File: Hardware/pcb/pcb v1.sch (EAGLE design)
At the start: 1 part, among them Y1 CFS206

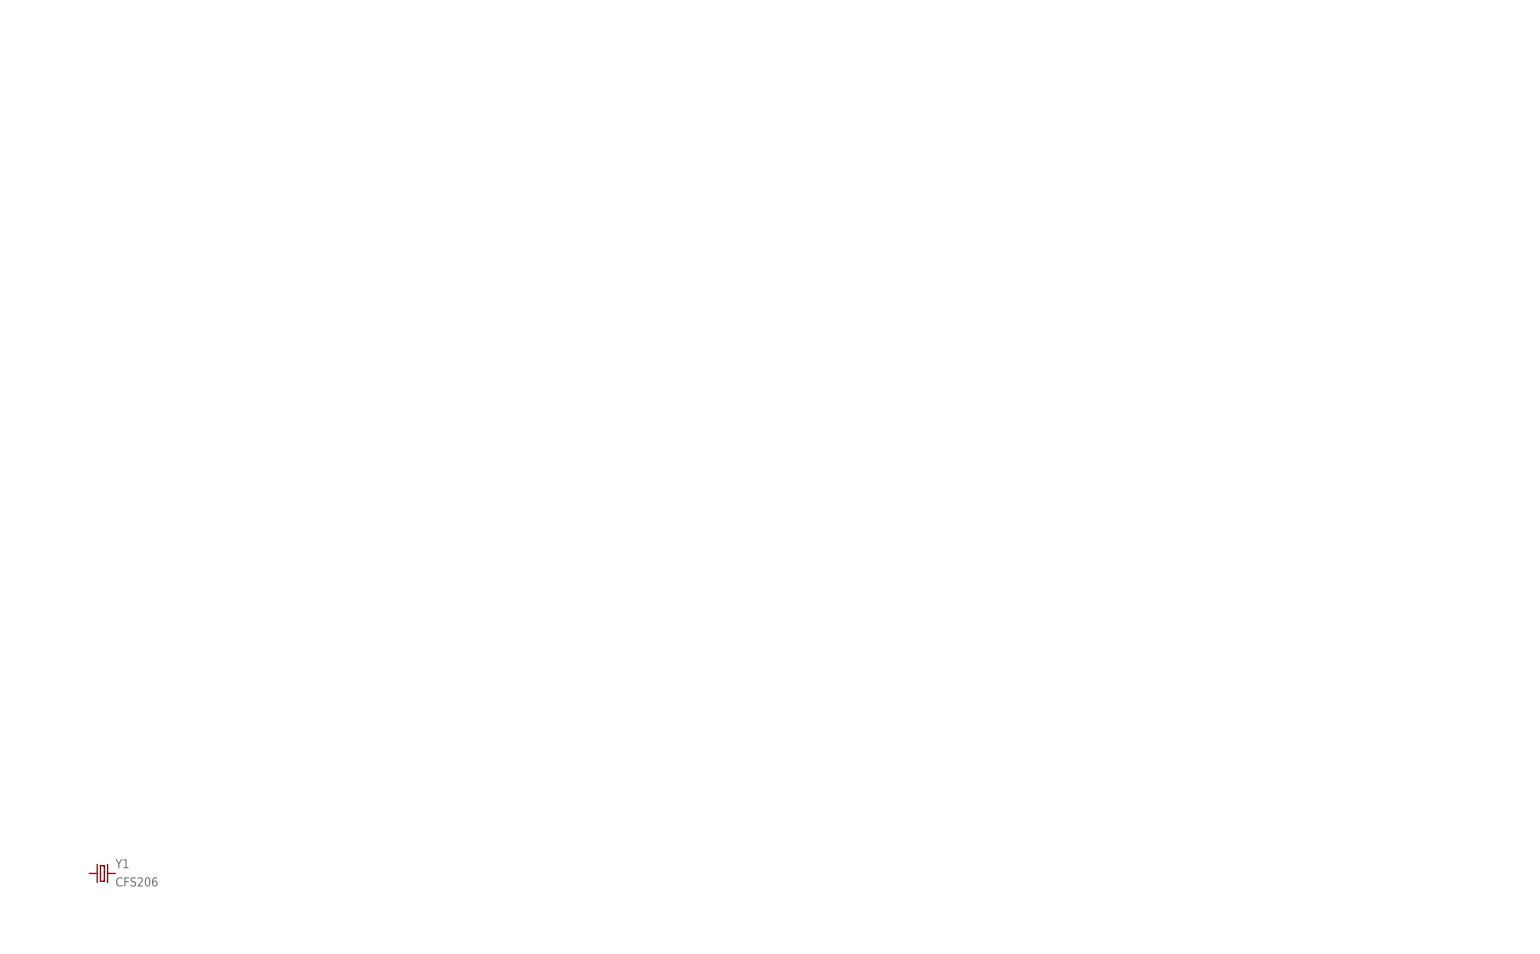
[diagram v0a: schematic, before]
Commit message: Perifericos agregados
Modulo Grove RFID
RTC
2 Reles
Regulador 3.3v
Buzzer
LED RGB
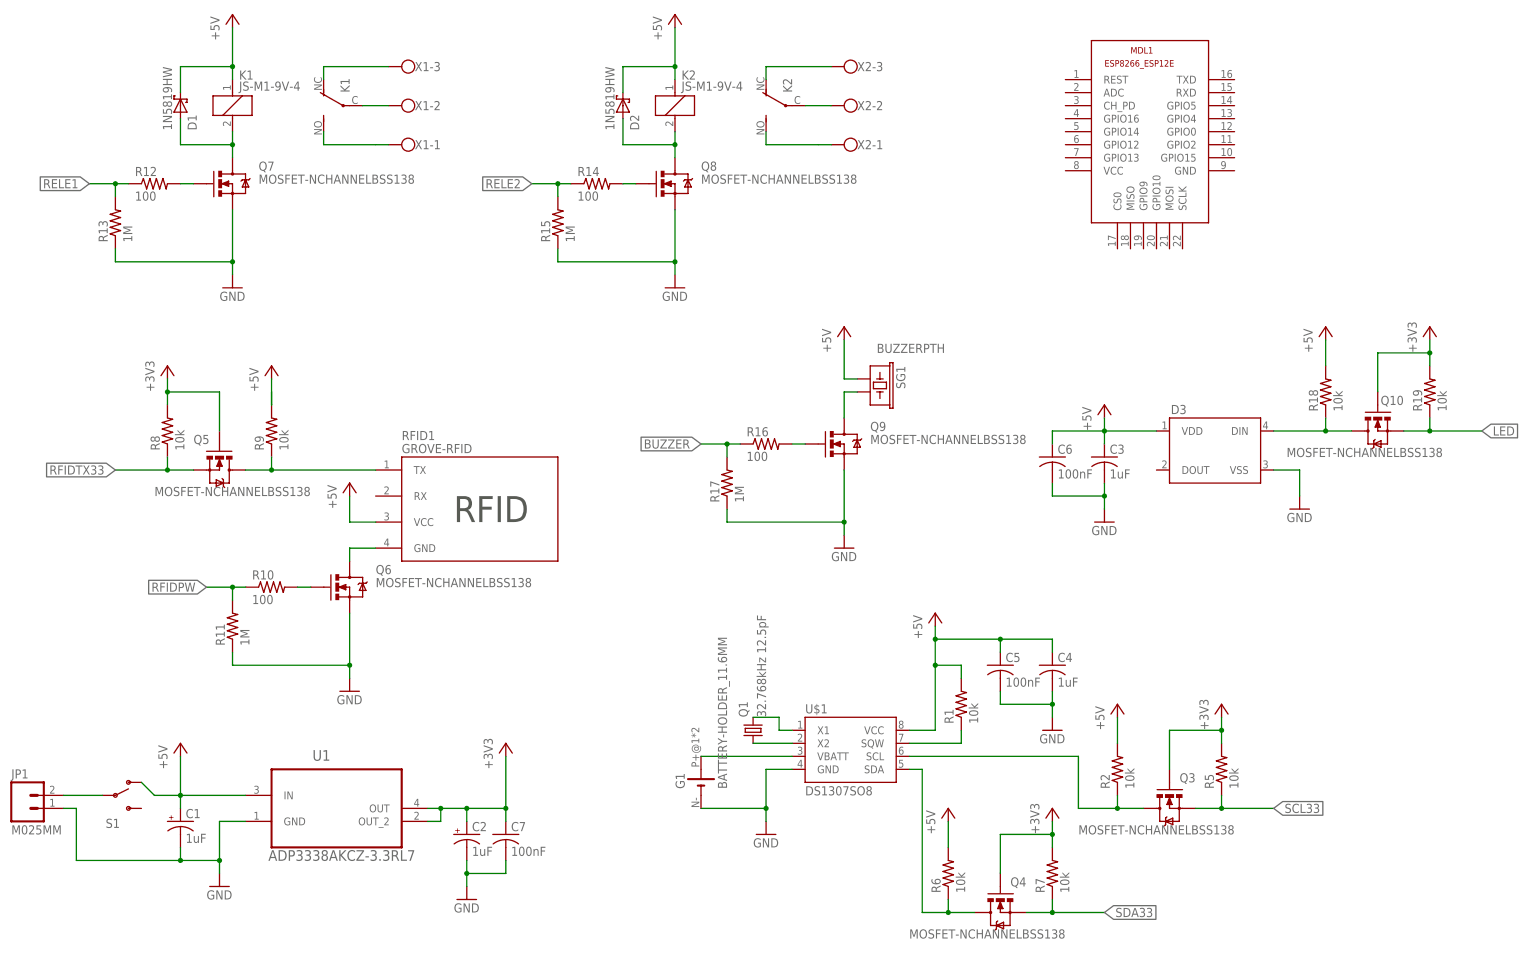
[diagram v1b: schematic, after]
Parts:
- removed Y1: CFS206, partes:CFS206
- added C1, C2: 1uF, rcl:CPOL-US150CLZ-1010
- added C3, C4: 1uF, rcl:C-USC0805
- added C5, C6, C7: 100nF, rcl:C-USC0805
- added D1, D2: 1N5819HW, diego:1N5819HW
- added D3: (no value), SparkFun-LED:WS2812B
- added G1: BATTERY-HOLDER_11.6MM, battery:BATTERY-HOLDER_11.6MM
- added JP1: M025MM, SparkFun-Connectors:M025MM
- added K1, K2: JS-M1-9V-4, relay:JS-M1-9V-4
- added MDL1: (no value), ESP8266-ESP12E:ESP8266-12EESP8266-ESP12E
- added Q1: 32.768kHz 12.5pF, crystal:CRYSTALTC26H
- added Q10, Q3, Q4, Q5, Q6, Q7, Q8, Q9: MOSFET-NCHANNELBSS138, SparkFun-DiscreteSemi:MOSFET-NCHANNELBSS138
- added R1, R18, R19, R2, R5, R6, R7, R8, R9: 10k, rcl:R-US_R0805
- added R10, R12, R14, R16: 100, rcl:R-US_R0805
- added R11, R13, R15, R17: 1M, rcl:R-US_R0805
- added RFID1: GROVE-RFID, partes:GROVE-RFID
- added S1: (no value), SparkFun-Electromechanical:SWITCH-SPDTPTH
- added SG1: BUZZERPTH, SparkFun-Electromechanical:BUZZERPTH
- added U$1: DS1307SO8, SparkFun-FreqCtrl:DS1307SO8
- added U1: ADP3338AKCZ-3.3RL7, ADI-Phase-2:ADP3338AKCZ-3.3RL7
- added X1, X2: (no value), con-wago-500:W237-103
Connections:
- new net +3V3: C2.+, C7.1, Q10.G, Q3.G, Q4.G, Q5.G, R19.2, R5.2, R7.2, R8.2, U1.OUT, U1.OUT_2
- new net +5V: C1.+, C3.1, C4.1, C5.1, C6.1, D1.C, D2.C, D3.VDD, K11.1, K21.1, R1.2, R18.2, R2.2, R6.2, R9.2, RFID1.VCC, S1.O, SG1.1, U$1.VCC, U1.IN
- new net BUZZER: R16.1, R17.2
- new net GND: C1.-, C2.-, C3.2, C4.2, C5.2, C6.2, C7.2, D3.VSS, G1.-, JP1.1, Q6.S, Q7.S, Q8.S, Q9.S, R11.1, R13.1, R15.1, R17.1, U$1.GND, U1.GND
- new net LED: Q10.S, R19.1
- new net N$1: JP1.2, S1.P
- new net N$11: Q5.D, R9.1, RFID1.TX
- new net N$12: D1.A, K11.2, Q7.D
- new net N$13: Q6.G, R10.2
- new net N$14: Q7.G, R12.2
- new net N$15: K12.O, X1-3.KL
- new net N$16: K12.P, X1-2.KL
- new net N$17: K12.S, X1-1.KL
- new net N$18: D2.A, K21.2, Q8.D
- new net N$19: Q8.G, R14.2
- new net N$2: Q1.2, U$1.X1
- new net N$20: K22.O, X2-3.KL
- new net N$21: K22.P, X2-2.KL
- new net N$22: K22.S, X2-1.KL
- new net N$23: Q9.G, R16.2
- new net N$24: Q9.D, SG1.2
- new net N$26: D3.DIN, Q10.D, R18.1
- new net N$3: Q1.1, U$1.X2
- new net N$4: G1.+, U$1.VBATT
- new net N$5: Q3.D, R2.1, U$1.SCL
- new net N$6: R1.1, U$1.SQW
- new net N$7: Q6.D, RFID1.GND
- new net N$9: Q4.D, R6.1, U$1.SDA
- new net RELE1: R12.1, R13.2
- new net RELE2: R14.1, R15.2
- new net RFIDPW: R10.1, R11.2
- new net RFIDTX33: Q5.S, R8.1
- new net SCL33: Q3.S, R5.1
- new net SDA33: Q4.S, R7.1
